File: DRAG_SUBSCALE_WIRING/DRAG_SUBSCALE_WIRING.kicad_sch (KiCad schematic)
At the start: 7 parts, among them J1 Screw_Terminal_01x02, SW1 SW_DPST_x2, U1 Teensy4.1

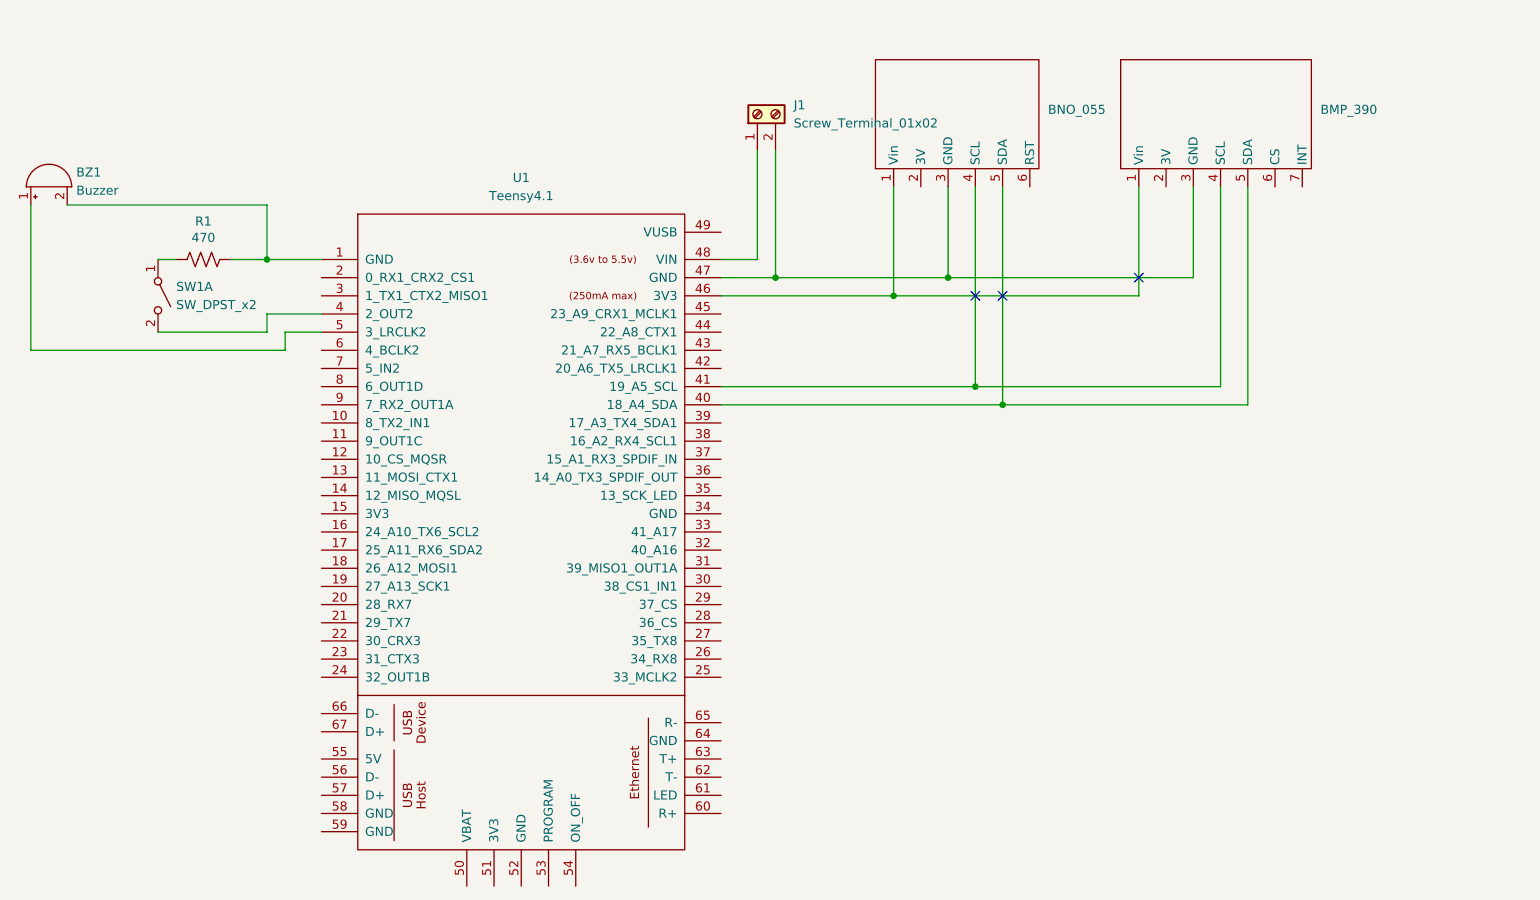
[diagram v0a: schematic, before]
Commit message: adding subscale flight data
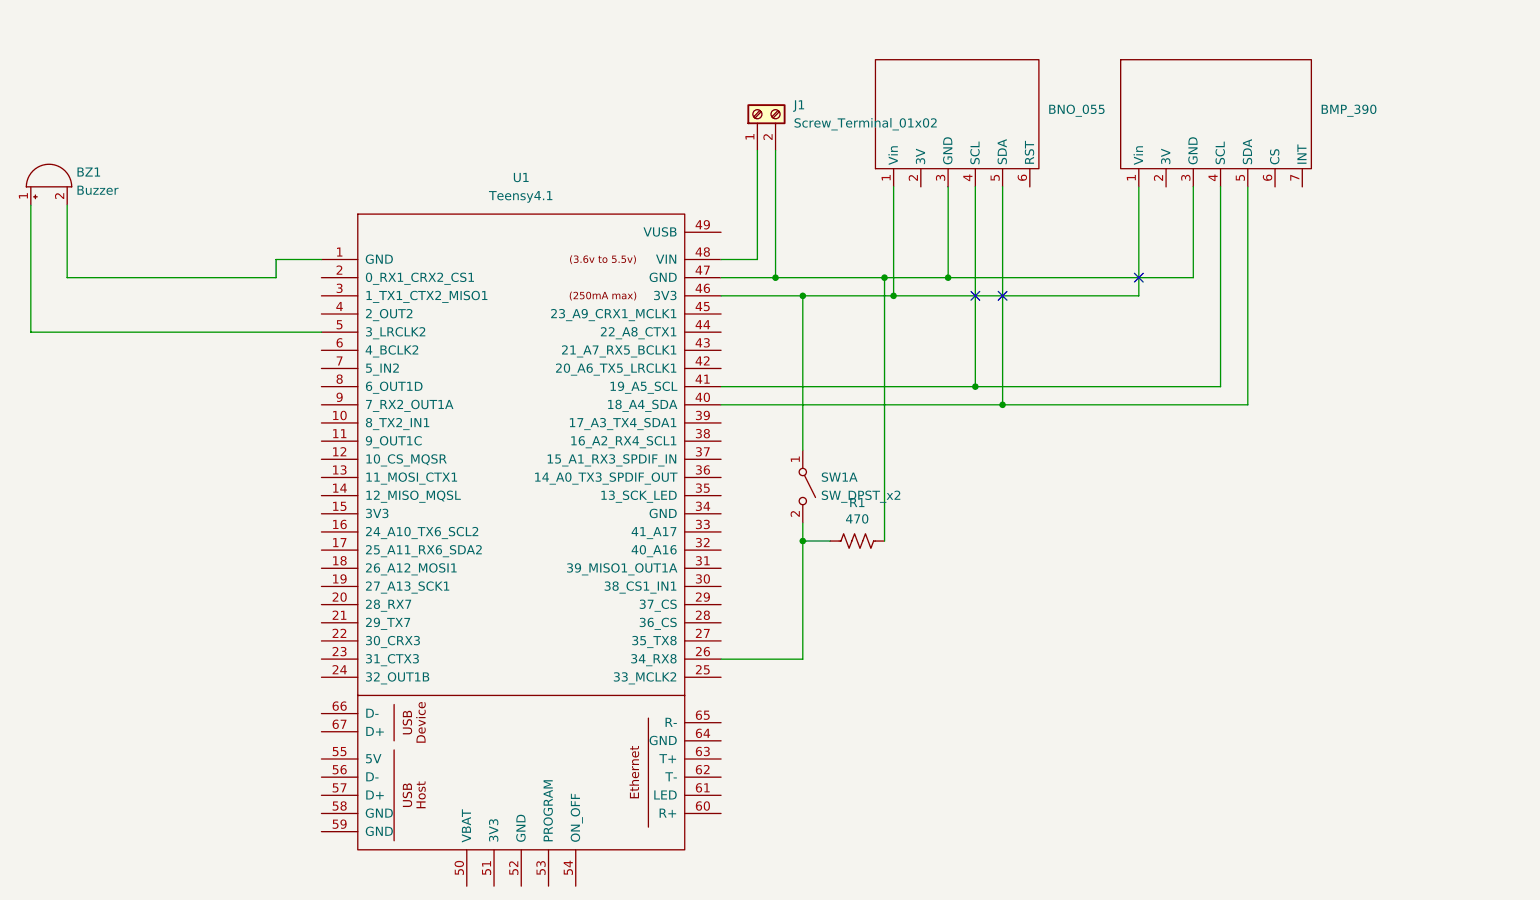
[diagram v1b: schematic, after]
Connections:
- net at BMP_390.1 (Vin), BNO_055.1 (Vin), U1.46 (3V3): now also SW1.1 (A)
- net at BMP_390.3 (GND), BNO_055.3 (GND), J1.2 (Pin_2)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: now also R1.2
- net at R1.1: now also SW1.2 (B), U1.26 (34_RX8); no longer SW1.1 (A)
- net at U1.4 (2_OUT2): no longer SW1.2 (B)
- net at BZ1.2 (-), U1.1 (GND): no longer R1.2
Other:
- moved on the sheet: R1, SW1A
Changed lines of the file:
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@@
+	)
+	(junction
+		(at 170.18 97.79)
+		(diameter 0)
+		(color 0 0 0 0)
+	)
+	(junction
+		(at 181.61 60.96)
+		(diameter 0)
+		(color 0 0 0 0)
 	)
 	(junction
@@
 	)
 	(junction
-		(at 194.31 76.2)
+		(at 170.18 63.5)
 		(diameter 0)
 		(color 0 0 0 0)
 	)
 	(junction
-		(at 95.25 58.42)
+		(at 194.31 76.2)
 		(diameter 0)
 		(color 0 0 0 0)
@@
 	(wire
 		(pts
+			(xy 67.31 60.96) (xy 96.52 60.96)
+		)
+		(stroke
+			(width 0)
+			(type default)
+		)
+	)
+	(wire
+		(pts
+			(xy 67.31 50.8) (xy 67.31 60.96)
+		)
+		(stroke
+			(width 0)
+			(type default)
+		)
+	)
+	(wire
+		(pts
 			(xy 158.75 76.2) (xy 194.31 76.2)
 		)
@@
 	(wire
 		(pts
-			(xy 102.87 66.04) (xy 95.25 66.04)
-		)
-		(stroke
-			(width 0)
-			(type default)
-		)
-	)
-	(wire
-		(pts
 			(xy 182.88 48.26) (xy 182.88 63.5)
 		)
@@
 	(wire
 		(pts
+			(xy 170.18 63.5) (xy 182.88 63.5)
+		)
+		(stroke
+			(width 0)
+			(type default)
+			(color 255 0 0 1)
+		)
+	)
+	(wire
+		(pts
 			(xy 217.17 48.26) (xy 217.17 63.5)
 		)
@@
 	(wire
 		(pts
-			(xy 97.79 68.58) (xy 97.79 71.12)
-		)
-		(stroke
-			(width 0)
-			(type default)
-		)
-	)
-	(wire
-		(pts
-			(xy 95.25 58.42) (xy 102.87 58.42)
-		)
-		(stroke
-			(width 0)
-			(type default)
-		)
-	)
-	(wire
-		(pts
-			(xy 62.23 71.12) (xy 97.79 71.12)
+			(xy 62.23 68.58) (xy 102.87 68.58)
 		)
 		(stroke
@@
 	(wire
 		(pts
+			(xy 170.18 97.79) (xy 173.99 97.79)
+		)
+		(stroke
+			(width 0)
+			(type default)
+		)
+	)
+	(wire
+		(pts
 			(xy 158.75 60.96) (xy 166.37 60.96)
 		)
@@
 	(wire
 		(pts
-			(xy 95.25 68.58) (xy 80.01 68.58)
-		)
-		(stroke
-			(width 0)
-			(type default)
-		)
-	)
-	(wire
-		(pts
-			(xy 97.79 68.58) (xy 102.87 68.58)
-		)
-		(stroke
-			(width 0)
-			(type default)
-		)
-	)
-	(wire
-		(pts
-			(xy 62.23 71.12) (xy 62.23 50.8)
-		)
-		(stroke
-			(width 0)
-			(type default)
-		)
-	)
-	(wire
-		(pts
-			(xy 95.25 66.04) (xy 95.25 68.58)
+			(xy 170.18 63.5) (xy 170.18 85.09)
+		)
+		(stroke
+			(width 0)
+			(type default)
+		)
+	)
+	(wire
+		(pts
+			(xy 62.23 68.58) (xy 62.23 50.8)
+		)
+		(stroke
+			(width 0)
+			(type default)
+		)
+	)
+	(wire
+		(pts
+			(xy 96.52 60.96) (xy 96.52 58.42)
 		)
 		(stroke
@@
 	(wire
 		(pts
-			(xy 90.17 58.42) (xy 95.25 58.42)
-		)
-		(stroke
-			(width 0)
-			(type default)
-		)
-	)
-	(wire
-		(pts
-			(xy 95.25 50.8) (xy 95.25 58.42)
-		)
-		(stroke
-			(width 0)
-			(type default)
+			(xy 181.61 60.96) (xy 190.5 60.96)
+		)
+		(stroke
+			(width 0)
+			(type default)
+			(color 0 0 0 1)
 		)
 	)
@@
 	(wire
 		(pts
-			(xy 67.31 50.8) (xy 95.25 50.8)
+			(xy 181.61 60.96) (xy 181.61 97.79)
 		)
 		(stroke
@@
 	(wire
 		(pts
-			(xy 166.37 60.96) (xy 190.5 60.96)
+			(xy 166.37 60.96) (xy 181.61 60.96)
 		)
 		(stroke
@@
 	(wire
 		(pts
-			(xy 80.01 58.42) (xy 82.55 58.42)
-		)
-		(stroke
-			(width 0)
-			(type default)
-		)
-	)
-	(wire
-		(pts
 			(xy 158.75 78.74) (xy 198.12 78.74)
 		)
@@
 	(wire
 		(pts
-			(xy 158.75 63.5) (xy 182.88 63.5)
+			(xy 158.75 114.3) (xy 170.18 114.3)
+		)
+		(stroke
+			(width 0)
+			(type default)
+		)
+	)
+	(wire
+		(pts
+			(xy 170.18 97.79) (xy 170.18 114.3)
+		)
+		(stroke
+			(width 0)
+			(type default)
+		)
+	)
+	(wire
+		(pts
+			(xy 158.75 63.5) (xy 170.18 63.5)
 		)
 		(stroke
@@
 			(type default)
 			(color 255 0 0 1)
+		)
+	)
+	(wire
+		(pts
+			(xy 96.52 58.42) (xy 102.87 58.42)
+		)
+		(stroke
+			(width 0)
+			(type default)
+		)
+	)
+	(wire
+		(pts
+			(xy 170.18 95.25) (xy 170.18 97.79)
+		)
+		(stroke
+			(width 0)
+			(type default)
 		)
 	)
@@
 	(symbol
 		(lib_id "Switch:SW_DPST_x2")
-		(at 80.01 63.5 270)
+		(at 170.18 90.17 270)
 		(unit 1)
 		(exclude_from_sim no)
@@
 		(fields_autoplaced yes)
 		(property "Reference" "SW1"
-			(at 82.55 62.2299 90)
+			(at 172.72 88.8999 90)
 			(effects
 				(font
@@
 		)
 		(property "Value" "SW_DPST_x2"
-			(at 82.55 64.7699 90)
+			(at 172.72 91.4399 90)
 			(effects
 				(font
@@
 		)
 		(property "Footprint" ""
-			(at 80.01 63.5 0)
+			(at 170.18 90.17 0)
 			(effects
 				(font
@@
 		)
 		(property "Datasheet" "~"
-			(at 80.01 63.5 0)
+			(at 170.18 90.17 0)
 			(effects
 				(font
@@
 		)
 		(property "Description" "Single Pole Single Throw (SPST) switch, separate symbol"
-			(at 80.01 63.5 0)
+			(at 170.18 90.17 0)
 			(effects
 				(font
@@
 	(symbol
 		(lib_id "Device:R_US")
-		(at 86.36 58.42 90)
+		(at 177.8 97.79 90)
 		(unit 1)
 		(exclude_from_sim no)
@@
 		(dnp no)
 		(property "Reference" "R1"
-			(at 86.36 53.086 90)
+			(at 177.8 92.456 90)
 			(effects
 				(font
@@
 		)
 		(property "Value" "470"
-			(at 86.36 55.372 90)
+			(at 177.8 94.742 90)
 			(effects
 				(font
@@
 		)
 		(property "Footprint" ""
-			(at 86.614 57.404 90)
+			(at 178.054 96.774 90)
 			(effects
 				(font
@@
 		)
 		(property "Datasheet" "~"
-			(at 86.36 58.42 0)
+			(at 177.8 97.79 0)
 			(effects
 				(font
@@
 		)
 		(property "Description" "Resistor, US symbol"
-			(at 86.36 58.42 0)
-			(effects
-				(font
+			(at 177.8 97.79 0)
+			(effects
+				(font

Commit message: worked on pcb and adding 3d models
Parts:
- removed J1: Screw_Terminal_01x02, symbol Connector:Screw_Terminal_01x02
- removed SW1: SW_DPST_x2, symbol Switch:SW_DPST_x2
- added H1, H2, H3, H4: MountingHole, MountingHole:MountingHole_3.2mm_M3_DIN965, symbol Mechanical:MountingHole
- added J1, J3: Conn_01x02, Connector_JST:JST_XA_B02B-XASK-1_1x02_P2.50mm_Vertical, symbol Connector_Generic:Conn_01x02
- BMP_390: footprint (none) -> Breakouts:BMP390
- BNO_055: footprint (none) -> Breakouts:BNO055Ada
- BZ1: footprint (none) -> Buzzer_Beeper:Buzzer_TDK_PS1240P02BT_D12.2mm_H6.5mm
- R1: footprint (none) -> Resistor_THT:R_Axial_DIN0411_L9.9mm_D3.6mm_P15.24mm_Horizontal
- U1: footprint (none) -> Breakouts:Teensy41
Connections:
- net 3v3: now reaches BMP_390.1 (Vin), BNO_055.1 (Vin), U1.46 (3V3)
- net 3v3: now also J3.1 (Pin_1)
- net GND: now reaches BMP_390.3 (GND), BNO_055.3 (GND), R1.2, U1.47 (GND)
- net GND: now also BZ1.2 (-), U1.1 (GND), J1.2 (Pin_2)
- net SCL: now reaches BMP_390.4 (SCL), BNO_055.4 (SCL), U1.41 (19_A5_SCL)
- net SDA: now reaches BNO_055.5 (SDA), U1.40 (18_A4_SDA)
- net SDA: now also BMP_390.6 (SDA); no longer BMP_390.5 (SDA)
- net at R1.1, U1.26 (34_RX8): now also J3.2 (Pin_2)
- net at U1.48 (VIN): now also J1.1 (Pin_1)
- no-connect marks 3 -> 0
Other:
- moved on the sheet: BNO_055, BZ1, R1
